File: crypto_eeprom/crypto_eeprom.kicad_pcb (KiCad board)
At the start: 2 copper layers, 12.8 x 10.2 mm, 3 parts, among them J1 EXPANSION_BOTTOM, U1 ATSHA204A

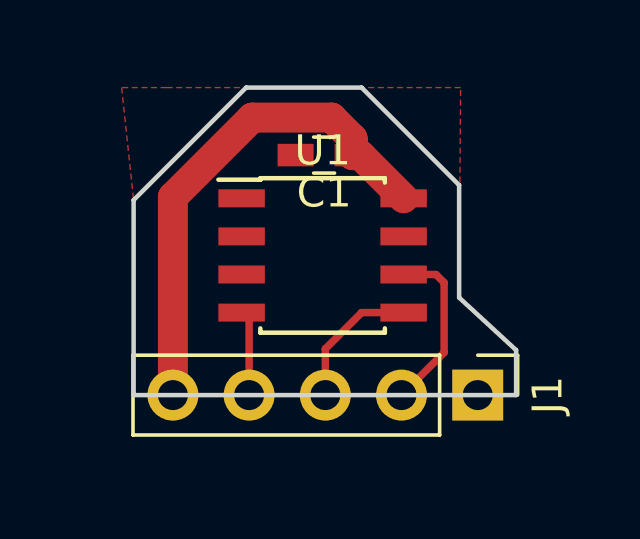
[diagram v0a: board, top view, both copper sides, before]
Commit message: Updated crypto_eeprom board to not interfere with USB shield contacts on back board
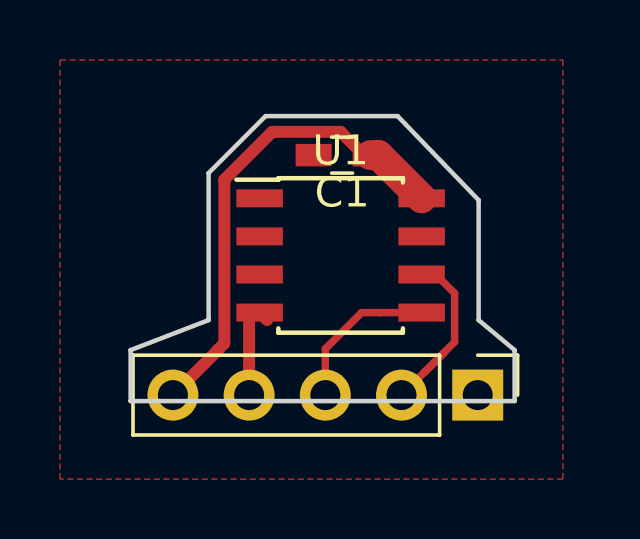
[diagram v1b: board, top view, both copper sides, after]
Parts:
- moved U1 0.60 mm to (148.8, 106.8)
- moved C1 0.60 mm to (148.8, 103.5)
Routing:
- net VCC: track 16.8 -> 16.0 mm
- net SCL: track 5.80 -> 6.41 mm
- net SDA: track 4.65 -> 5.25 mm
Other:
- board size 12.8 x 10.2 mm -> 12.8 x 9.5 mm
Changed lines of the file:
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@@
     (links 6)
     (no_connects 0)
-    (area 139.905 101.025 156.775 119.104762)
+    (area 101.646 69.33 118.975 88.104762)
     (thickness 1.6)
-    (drawings 9)
-    (tracks 16)
+    (drawings 11)
+    (tracks 22)
     (zones 0)
     (modules 3)
@@
   )
   (setup
-    (last_trace_width 0.25)
+    (last_trace_width 0.4)
     (user_trace_width 0.25)
     (user_trace_width 0.4)
@@
     (pad_to_mask_clearance 0.2)
     (aux_axis_origin 141.2875 101.1555)
-    (visible_elements 7FFFFFFF)
+    (visible_elements 7FFFFF7F)
     (pcbplotparams
       (layerselection 0x010f0_80000001)
@@
   )
   (module Capacitors_SMD:C_0603_HandSoldering (layer F.Cu)
-    (at 148.25 103.5 180)
+    (at 148.85 103.5 180)
     (descr "Capacitor SMD 0603, hand soldering")
     (tags "capacitor 0603")
@@
     (descr "Through hole straight pin header, 1x05, 2.54mm pitch, single row")
     (tags "Through hole pin header THT 1x05 2.54mm single row")
-    (fp_text reference J1 (at 0 -2.33 270) (layer F.SilkS)
-      (effects (font (size 1 1) (thickness 0.15)))
-    )
-    (fp_text value EXPANSION_BOTTOM (at 0 12.49 270) (layer F.Fab)
+    (fp_text reference J1 (at 0 -2.33 270) (layer F.SilkS) hide
+      (effects (font (size 1 1) (thickness 0.15)))
+    )
+    (fp_text value EXPANSION_BOTTOM (at 0 12.49 270) (layer F.Fab) hide
       (effects (font (size 1 1) (thickness 0.15)))
     )
@@
     (fp_line (start 1.8 11.95) (end 1.8 -1.8) (layer F.CrtYd) (width 0.05))
     (fp_line (start 1.8 -1.8) (end -1.8 -1.8) (layer F.CrtYd) (width 0.05))
-    (fp_text user %R (at 0 -2.33 270) (layer F.Fab)
+    (fp_text user %R (at 0 -2.33 270) (layer F.Fab) hide
       (effects (font (size 1 1) (thickness 0.15)))
     )
@@
   )
   (module Housings_SOIC:SOIC-8_3.9x4.9mm_Pitch1.27mm (layer F.Cu)
-    (at 148.2 106.845)
+    (at 148.8 106.845)
     (descr "8-Lead Plastic Small Outline (SN) - Narrow, 3.90 mm Body [SOIC] (see Microchip Packaging Specification 00000049BS.pdf)")
     (tags "SOIC 1.27")
@@
       (effects (font (size 1 1) (thickness 0.15)))
     )
-    (fp_text value ATSHA204A (at 0 3.5) (layer F.Fab)
-      (effects (font (size 1 1) (thickness 0.15)))
-    )
-    (fp_text user %R (at 0 0) (layer F.Fab)
+    (fp_text value ATSHA204A (at 0 3.5) (layer F.Fab) hide
+      (effects (font (size 1 1) (thickness 0.15)))
+    )
+    (fp_text user %R (at 0 0) (layer F.Fab) hide
       (effects (font (size 1 1) (thickness 0.15)))
     )
@@
     )
   )
-  (gr_text "ATSHA204\nZeroPhone\nmod " (at 147.7 106.2 180) (layer B.SilkS)
-    (effects (font (size 1.5 1.2) (thickness 0.2)) (justify mirror))
-  )
-  (gr_line (start 154.65 111.5) (end 154.65 110) (layer Edge.Cuts) (width 0.15))
-  (gr_line (start 141.9 111.5) (end 154.65 111.5) (layer Edge.Cuts) (width 0.15))
-  (gr_line (start 145.65 101.25) (end 141.9 105) (layer Edge.Cuts) (width 0.15))
-  (gr_line (start 152.75 108.25) (end 154.65 110) (layer Edge.Cuts) (width 0.15))
-  (gr_line (start 152.75 104.5) (end 152.75 108.25) (layer Edge.Cuts) (width 0.15))
-  (gr_line (start 149.5 101.25) (end 152.75 104.5) (layer Edge.Cuts) (width 0.15))
-  (gr_line (start 141.9 105) (end 141.9 111.5) (layer Edge.Cuts) (width 0.15))
-  (gr_line (start 149.5 101.25) (end 145.65 101.25) (layer Edge.Cuts) (width 0.15))
-  (segment (start 149.2 103.5) (end 149.46 103.5) (width 1) (layer F.Cu) (net 1))
-  (segment (start 149.46 103.5) (end 150.9 104.94) (width 1) (layer F.Cu) (net 1))
-  (segment (start 148.5 102.25) (end 149.2 102.95) (width 1) (layer F.Cu) (net 1))
-  (segment (start 149.2 102.95) (end 149.2 103.5) (width 1) (layer F.Cu) (net 1))
-  (segment (start 145.854998 102.25) (end 148.5 102.25) (width 1) (layer F.Cu) (net 1))
-  (segment (start 143.21 111.5) (end 143.21 104.894998) (width 1) (layer F.Cu) (net 1))
-  (segment (start 143.21 104.894998) (end 145.854998 102.25) (width 1) (layer F.Cu) (net 1))
-  (segment (start 145.75 111.5) (end 145.75 109) (width 0.25) (layer F.Cu) (net 2))
-  (segment (start 145.75 109) (end 145.5 108.75) (width 0.25) (layer F.Cu) (net 2))
-  (segment (start 152.25 107.75) (end 151.98 107.48) (width 0.25) (layer F.Cu) (net 3))
-  (segment (start 151.98 107.48) (end 150.9 107.48) (width 0.25) (layer F.Cu) (net 3))
-  (segment (start 152.25 110.08) (end 152.25 107.75) (width 0.25) (layer F.Cu) (net 3))
-  (segment (start 150.83 111.5) (end 152.25 110.08) (width 0.25) (layer F.Cu) (net 3))
+  (gr_line (start 153.4 105) (end 153.4 109) (layer Edge.Cuts) (width 0.15))
+  (gr_line (start 150.7 102.2) (end 153.4 105) (layer Edge.Cuts) (width 0.15))
+  (gr_line (start 146.3 102.2) (end 150.7 102.2) (layer Edge.Cuts) (width 0.15))
+  (gr_line (start 144.4 104.1) (end 146.3 102.2) (layer Edge.Cuts) (width 0.15))
+  (gr_line (start 144.4 109) (end 144.4 104.1) (layer Edge.Cuts) (width 0.15))
+  (gr_line (start 141.8 110) (end 144.4 109) (layer Edge.Cuts) (width 0.15))
+  (gr_line (start 141.8 111.7) (end 141.8 110) (layer Edge.Cuts) (width 0.15))
+  (gr_line (start 154.6 110) (end 153.4 109) (layer Edge.Cuts) (width 0.15))
+  (gr_line (start 154.6 111.7) (end 154.6 110) (layer Edge.Cuts) (width 0.15))
+  (gr_text "ATSHA204\nZeroPhone\nmod " (at 148.8344 106.2736 180) (layer B.SilkS)
+    (effects (font (size 1 1) (thickness 0.2)) (justify mirror))
+  )
+  (gr_line (start 141.8 111.7) (end 154.6 111.7) (layer Edge.Cuts) (width 0.15))
+  (segment (start 143.21 111.5) (end 144.7 110.01) (width 0.4) (layer F.Cu) (net 1))
+  (segment (start 144.7 110.01) (end 144.7 110) (width 0.4) (layer F.Cu) (net 1))
+  (segment (start 144.7 110) (end 144.924999 109.775001) (width 0.4) (layer F.Cu) (net 1))
+  (segment (start 144.924999 109.775001) (end 144.924999 104.319999) (width 0.4) (layer F.Cu) (net 1))
+  (segment (start 144.924999 104.319999) (end 146.519999 102.724999) (width 0.4) (layer F.Cu) (net 1))
+  (segment (start 146.519999 102.724999) (end 148.8 102.725) (width 0.4) (layer F.Cu) (net 1))
+  (segment (start 148.8 102.725) (end 149.575 103.5) (width 0.4) (layer F.Cu) (net 1))
+  (segment (start 149.575 103.5) (end 149.8 103.5) (width 0.4) (layer F.Cu) (net 1))
+  (segment (start 149.8 103.5) (end 150.06 103.5) (width 1) (layer F.Cu) (net 1))
+  (segment (start 150.06 103.5) (end 151.5 104.94) (width 1) (layer F.Cu) (net 1))
+  (segment (start 145.75 111.5) (end 145.75 109) (width 0.4) (layer F.Cu) (net 2))
+  (segment (start 146.35 109) (end 146.1 108.75) (width 0.4) (layer F.Cu) (net 2))
+  (segment (start 150.83 111.5) (end 151.6 110.73) (width 0.25) (layer F.Cu) (net 3))
+  (segment (start 151.6 110.73) (end 152.25 110.08) (width 0.25) (layer F.Cu) (net 3))
+  (segment (start 151.5 107.48) (end 151.975 107.48) (width 0.25) (layer F.Cu) (net 3))
+  (segment (start 151.975 107.48) (end 152.600001 108.105001) (width 0.25) (layer F.Cu) (net 3))
+  (segment (start 152.600001 108.105001) (end 152.600001 109.729999) (width 0.25) (layer F.Cu) (net 3))
+  (segment (start 152.600001 109.729999) (end 151.6 110.73) (width 0.25) (layer F.Cu) (net 3))
+  (segment (start 149.5 108.75) (end 150.1 108.75) (width 0.25) (layer F.Cu) (net 4))
   (segment (start 149.5 108.75) (end 148.29 109.96) (width 0.25) (layer F.Cu) (net 4))
   (segment (start 148.29 109.96) (end 148.29 111.5) (width 0.25) (layer F.Cu) (net 4))
-  (segment (start 150.9 108.75) (end 149.5 108.75) (width 0.25) (layer F.Cu) (net 4))
+  (segment (start 151.5 108.75) (end 150.1 108.75) (width 0.25) (layer F.Cu) (net 4))
   (zone (net 2) (net_name GND) (layer F.Cu) (hatch edge 0.508)
-    (connect_pads (clearance 0.25))
-    (min_thickness 0.16)
-    (fill yes (arc_segments 16) (thermal_gap 0.25) (thermal_bridge_width 0.5))
+    (connect_pads (clearance 0.2))
+    (min_thickness 0.2)
+    (fill yes (arc_segments 16) (thermal_gap 0.2) (thermal_bridge_width 0.24))
     (polygon
       (pts
-        (xy 141.9 105) (xy 141.9 111.5) (xy 154.65 111.5) (xy 154.65 110) (xy 152.75 108.25)
-        (xy 152.8 101.25) (xy 143 101.25) (xy 141.5 101.25)
+        (xy 139.446 100.33) (xy 156.21 100.33) (xy 156.21 114.3) (xy 139.446 114.3)
       )
     )
